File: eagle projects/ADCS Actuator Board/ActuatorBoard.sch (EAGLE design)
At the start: 259 parts, among them J4 OSTVN08A150, J5 OSTVN08A150, J6 OSTVN08A150, U10 TVS991, U11 BD6210F-E2, U12 ADS7841E_2K5, U13 ADS7841E_2K5, U15 TLV9051IDCKR, U16 BD6210F-E2, U17 DRV10970_MOTOR_DRIVERDRV10970, U18 DRV10970_MOTOR_DRIVERDRV10970, U19 TLV9051IDCKR, U20 DRV10970_MOTOR_DRIVERDRV10970, U21 TLV9051IDCKR, U22 BD6210F-E2, U23 TLV9051IDCKR, U24 TLV9051IDCKR, U25 ADS7841E_2K5, U26 TLV9051IDCKR, U27 ADS7841E_2K5, U28 TLV9051IDCKR, U29 TLV9051IDCKR, U30 TLV9051IDCKR, U31 TLV9051IDCKR, U32 TLV9051IDCKR, U4 ADS7841E_2K5, U6 TLV9051IDCKR, U7 TVS991, U8 TVS991, U9 ADS7841E_2K5

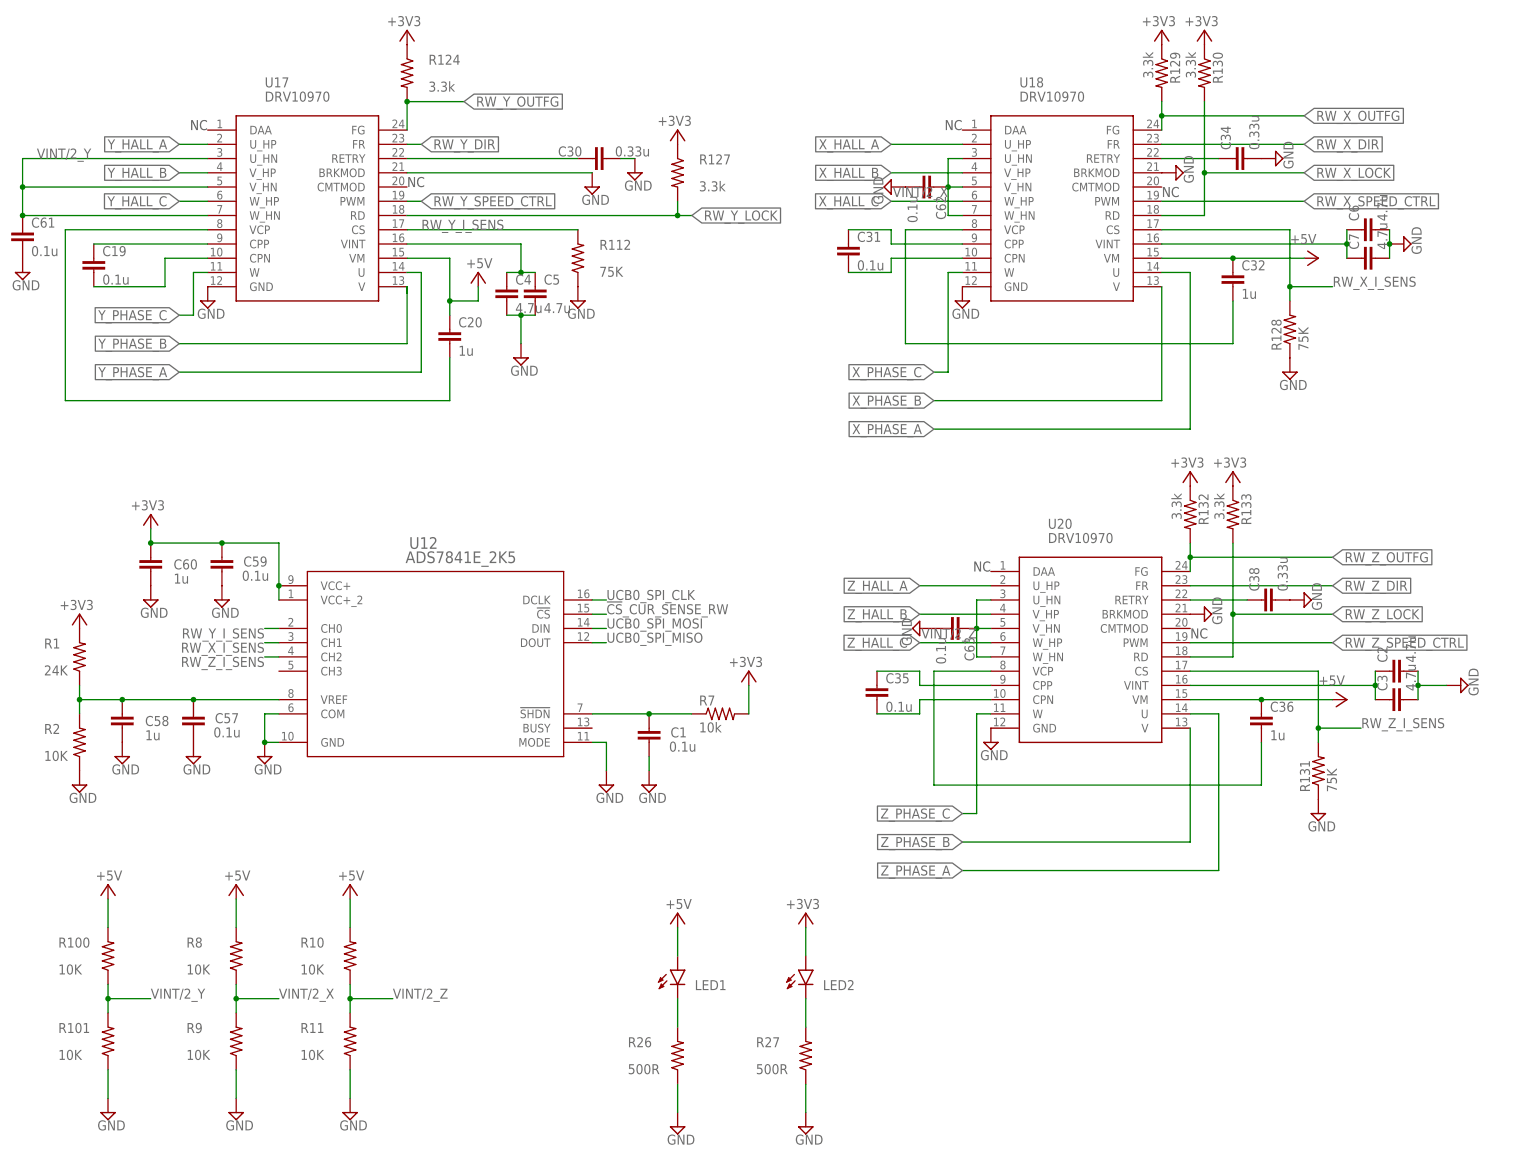
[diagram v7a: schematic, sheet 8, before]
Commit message: Fixed motordriver schematic for readability
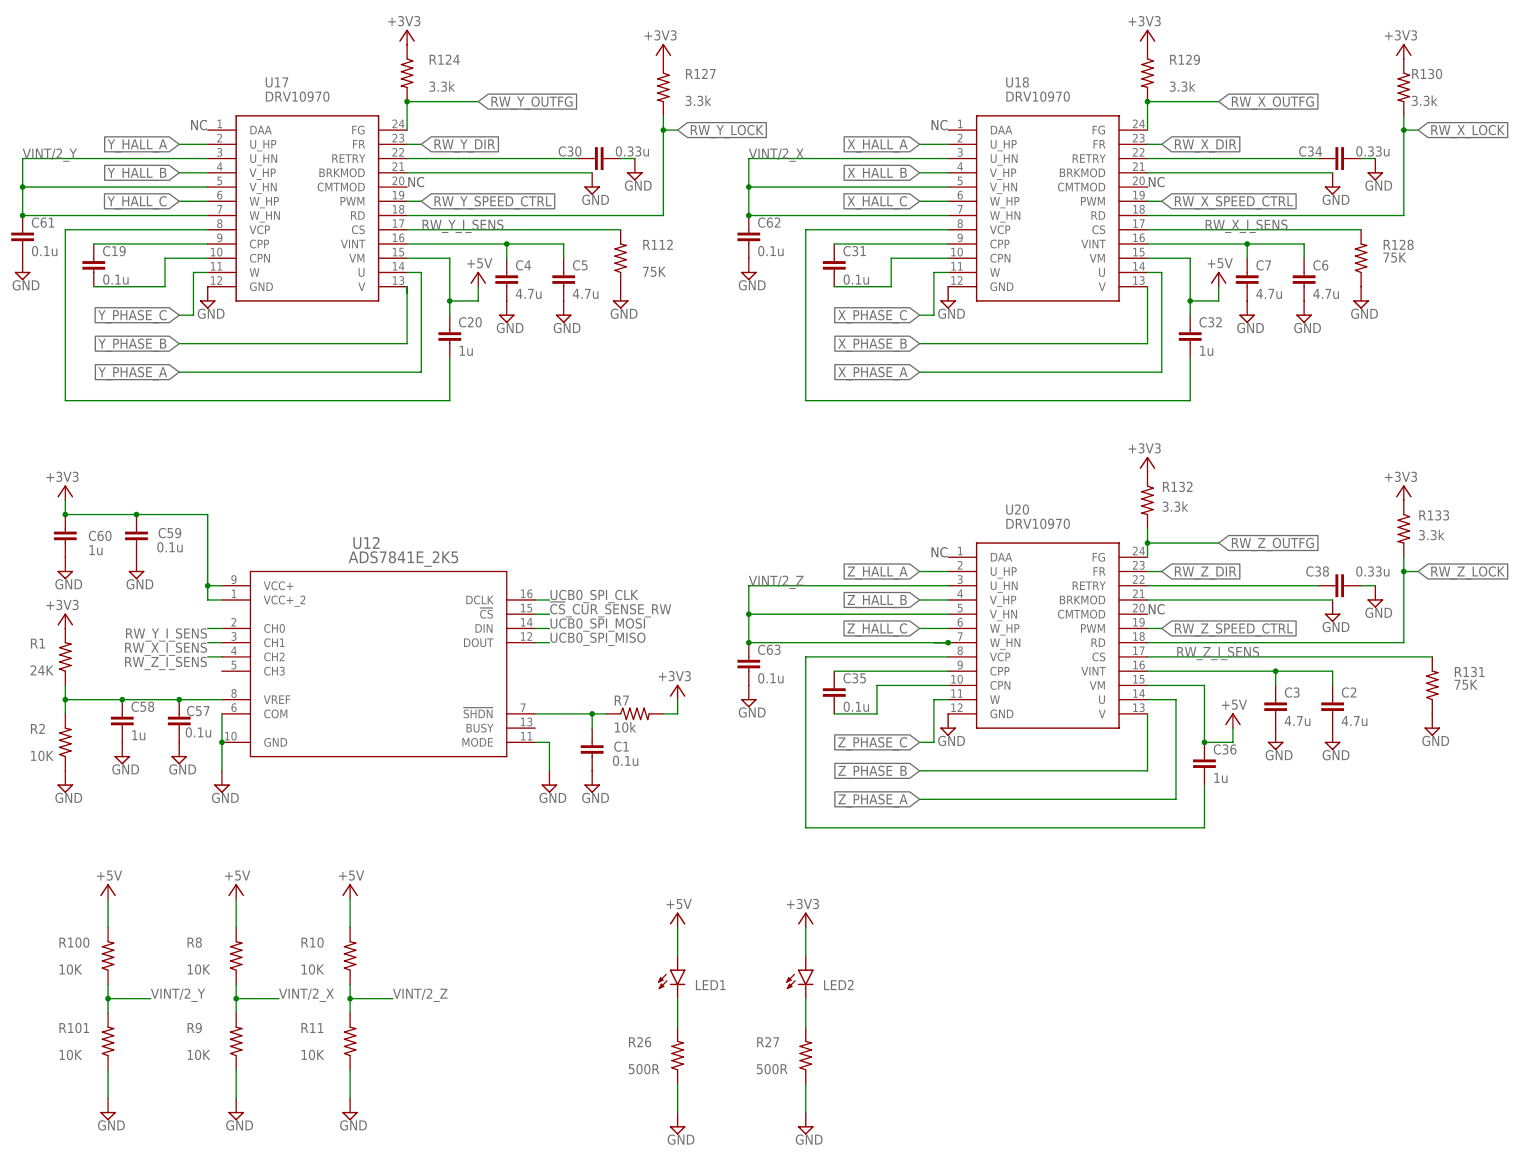
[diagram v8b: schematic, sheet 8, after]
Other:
- moved on the sheet: C1, C2, C3, C31, C32, C34, C35, C36, C38, C4, C5, C57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
